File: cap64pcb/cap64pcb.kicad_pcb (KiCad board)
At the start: 2 copper layers, 91.6 x 12 mm, 31 parts, among them J1 SM04B_SURS_TF, Q1 BSS138, Q2 BSS138, U1 MPR121QR2, U2 SPX3819-3.3

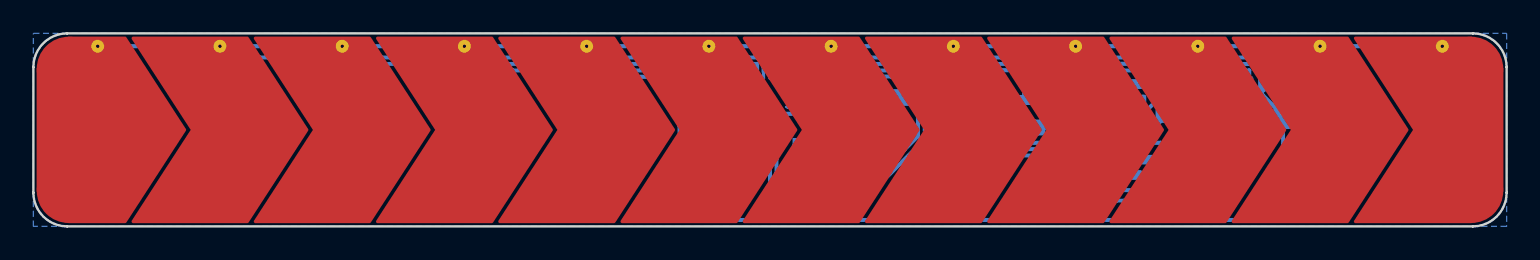
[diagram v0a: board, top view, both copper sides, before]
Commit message: half filleted
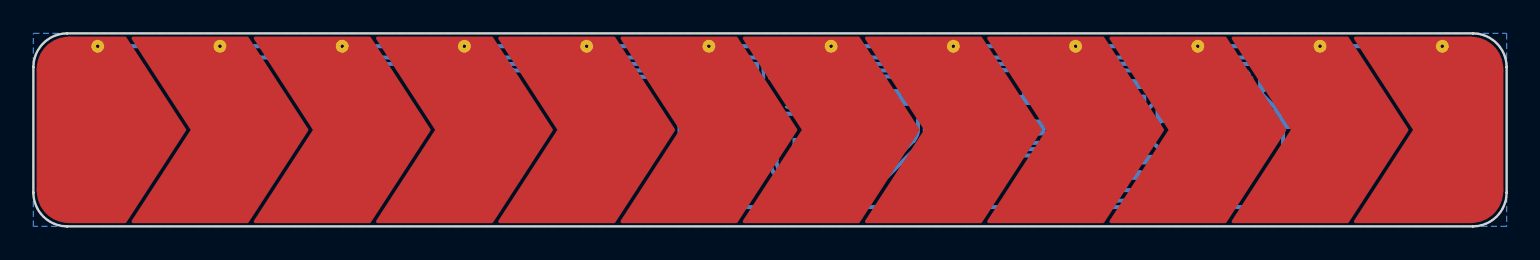
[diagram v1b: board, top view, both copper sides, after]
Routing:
- net GND: track 86.7 -> 82.9 mm
- net Net-(J1-Pad3): track 20.8 -> 19.0 mm
- net Net-(J1-Pad4): track 8.71 -> 7.77 mm
- net SDA: track 28.1 -> 27.5 mm
- net SCL: track 31.5 -> 31.0 mm

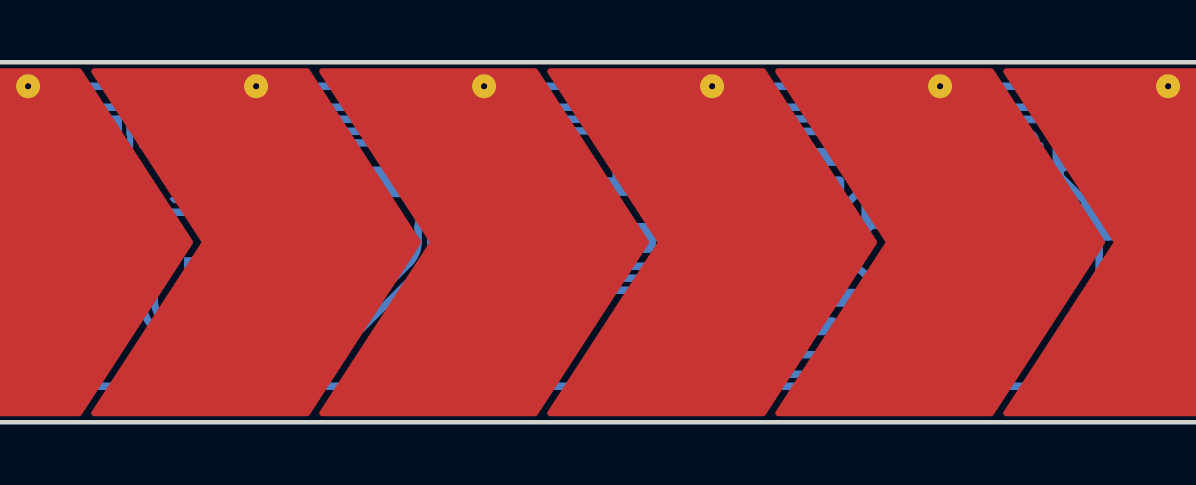
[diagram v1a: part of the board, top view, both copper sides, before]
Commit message: shifted caps/resistors up a smidge
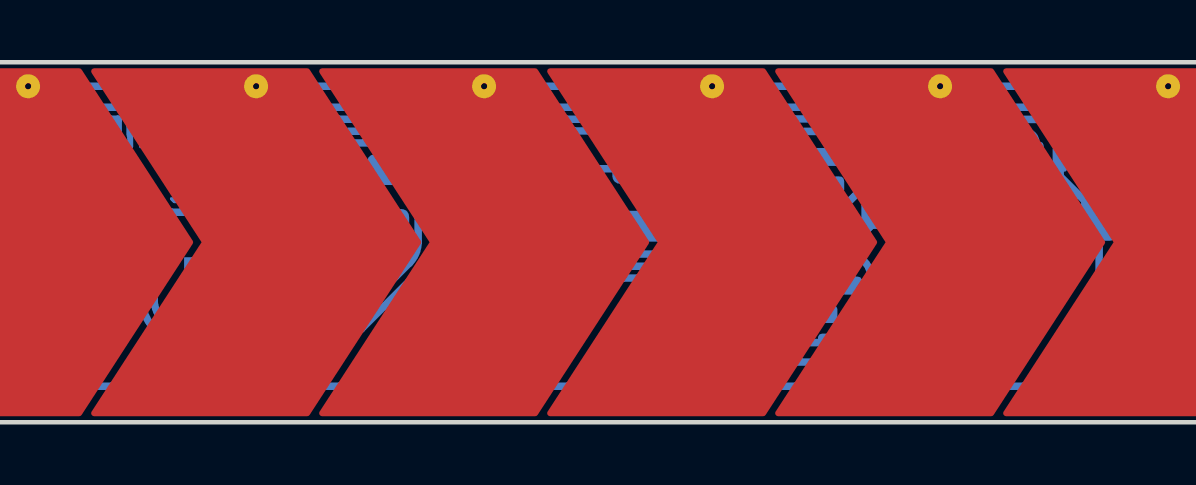
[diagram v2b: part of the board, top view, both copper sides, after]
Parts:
- moved C2 0.41 mm to (98.5, 43.5)
- moved C3 0.41 mm to (96.4, 43.5)
- moved C4 0.41 mm to (94.3, 43.5)
- moved D1 0.41 mm to (85.4, 43.6)
- moved R2 0.41 mm to (92.2, 43.5)
- moved R3 0.41 mm to (90.2, 43.5)
- moved R4 0.41 mm to (88.2, 43.5)
- moved Q1 0.41 mm to (101.5, 47.4)
- moved Q2 0.41 mm to (104.2, 47.4)
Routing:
- net Net-(J1-Pad3): track 19.0 -> 19.9 mm
- net +3V3: track 42.4 -> 43.2 mm
- net Net-(J1-Pad4): track 7.77 -> 8.31 mm

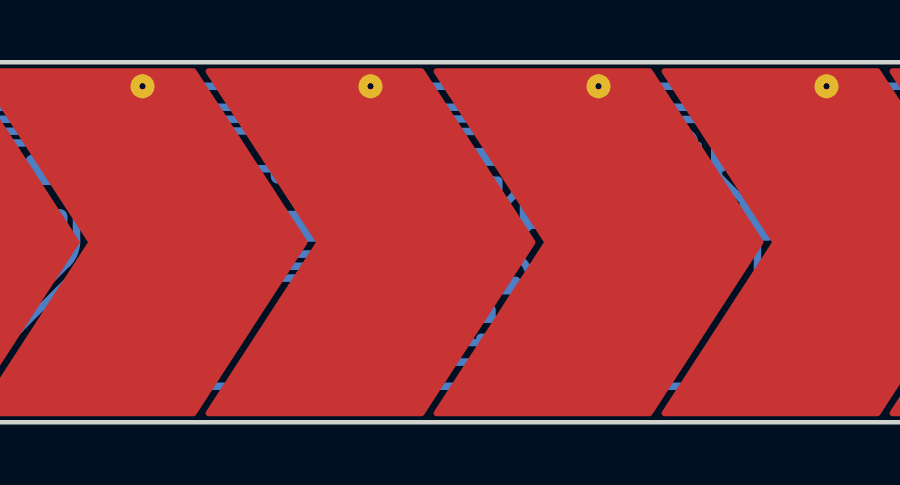
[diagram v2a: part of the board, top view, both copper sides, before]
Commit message: reconnect cap gnd pins
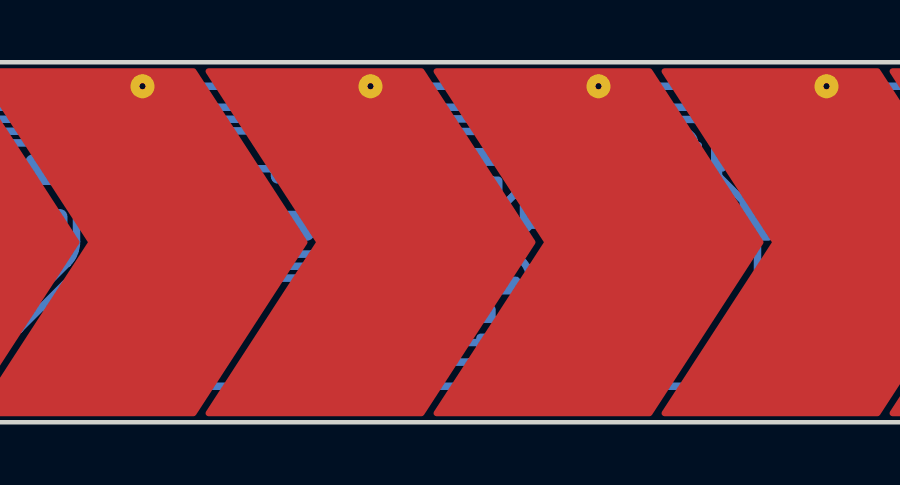
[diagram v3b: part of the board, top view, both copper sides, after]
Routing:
- net Net-(J1-Pad3): track 19.9 -> 18.6 mm
- net Net-(J1-Pad4): track 8.31 -> 7.37 mm
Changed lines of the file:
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@@
   (segment (start 104.7 44.055723) (end 104.05 44.705723) (width 0.25) (layer "B.Cu") (net 2))
   (segment (start 74.45 47.4) (end 75.4 47.4) (width 0.25) (layer "B.Cu") (net 2))
+  (segment (start 101.6 44.705723) (end 98.755723 44.705723) (width 0.25) (layer "B.Cu") (net 2))
   (segment (start 74.45 45.4) (end 74.75 45.1) (width 0.25) (layer "B.Cu") (net 2))
-  (segment (start 101.6 44.705723) (end 101.45 44.855723) (width 0.25) (layer "B.Cu") (net 2))
+  (segment (start 98.5 44.45) (end 96.4 44.45) (width 0.25) (layer "B.Cu") (net 2))
   (segment (start 75.6875 44.1) (end 74.7875 43.2) (width 0.25) (layer "B.Cu") (net 2))
   (segment (start 104.744277 44.1) (end 104.7 44.055723) (width 0.25) (layer "B.Cu") (net 2))
   (segment (start 107.294277 41.305723) (end 101.6 41.305723) (width 0.25) (layer "B.Cu") (net 2))
+  (segment (start 98.755723 44.705723) (end 98.5 44.45) (width 0.25) (layer "B.Cu") (net 2))
   (segment (start 78.1125 44.1) (end 75.6875 44.1) (width 0.25) (layer "B.Cu") (net 2))
   (segment (start 104.05 44.705723) (end 101.6 44.705723) (width 0.25) (layer "B.Cu") (net 2))
+  (segment (start 96.4 44.45) (end 94.3 44.45) (width 0.25) (layer "B.Cu") (net 2))
   (segment (start 110.6 42.15) (end 110.6 42.8) (width 0.25) (layer "B.Cu") (net 2))
   (segment (start 107.694277 40.905723) (end 107.294277 41.305723) (width 0.25) (layer "B.Cu") (net 2))
   (segment (start 74.45 47.4) (end 74.45 45.4) (width 0.25) (layer "B.Cu") (net 2))
   (segment (start 102.7375 43.105723) (end 101.6 43.105723) (width 0.25) (layer "B.Cu") (net 2))
-  (segment (start 96.4 44.855723) (end 94.3 44.855723) (width 0.25) (layer "B.Cu") (net 2))
   (segment (start 74.75 45.0375) (end 75.6875 44.1) (width 0.25) (layer "B.Cu") (net 2))
-  (segment (start 101.45 44.855723) (end 98.5 44.855723) (width 0.25) (layer "B.Cu") (net 2))
   (segment (start 110.6 42.8) (end 111.9 44.1) (width 0.25) (layer "B.Cu") (net 2))
-  (segment (start 98.5 44.855723) (end 96.4 44.855723) (width 0.25) (layer "B.Cu") (net 2))
   (segment (start 111.9 44.1) (end 111.9 47.8) (width 0.25) (layer "B.Cu") (net 2))
   (segment (start 106.9 44.1) (end 104.744277 44.1) (width 0.25) (layer "B.Cu") (net 2))
@@
   (segment (start 103.892893 48.994277) (end 100 48.994277) (width 0.25) (layer "B.Cu") (net 6))
   (segment (start 99.5 48.494277) (end 99.5 47.894277) (width 0.25) (layer "B.Cu") (net 6))
-  (segment (start 109 42.15) (end 109 48.194277) (width 0.25) (layer "B.Cu") (net 6))
+  (segment (start 109 42.15) (end 109 45.394277) (width 0.25) (layer "B.Cu") (net 6))
   (segment (start 100 47.394277) (end 102.4375 47.394277) (width 0.25) (layer "B.Cu") (net 6))
-  (segment (start 109 48.194277) (end 105.107107 48.194277) (width 0.25) (layer "B.Cu") (net 6))
+  (segment (start 106.2 48.194277) (end 105.107107 48.194277) (width 0.25) (layer "B.Cu") (net 6))
   (arc (start 104.246447 48.84783) (mid 104.084235 48.956217) (end 103.892893 48.994277) (width 0.25) (layer "B.Cu") (net 6))
   (arc (start 100 48.994277) (mid 99.646447 48.84783) (end 99.5 48.494277) (width 0.25) (layer "B.Cu") (net 6))
   (arc (start 99.5 47.894277) (mid 99.646447 47.540724) (end 100 47.394277) (width 0.25) (layer "B.Cu") (net 6))
+  (arc (start 109 45.394277) (mid 108.179899 47.374176) (end 106.2 48.194277) (width 0.25) (layer "B.Cu") (net 6))
   (arc (start 105.107107 48.194277) (mid 104.915766 48.232337) (end 104.753554 48.340723) (width 0.25) (layer "B.Cu") (net 6))
   (segment (start 79 47.4) (end 79.5 46.9) (width 0.25) (layer "B.Cu") (net 7))
@@
   (segment (start 86.3375 43.594277) (end 86.973286 43.594277) (width 0.25) (layer "B.Cu") (net 23))
   (arc (start 87.680393 43.88717) (mid 87.35597 43.670397) (end 86.973286 43.594277) (width 0.25) (layer "B.Cu") (net 23))
-  (segment (start 108.2 42.15) (end 108.2 47.394277) (width 0.25) (layer "B.Cu") (net 24))
-  (segment (start 108.2 47.394277) (end 105.137501 47.394277) (width 0.25) (layer "B.Cu") (net 24))
+  (segment (start 108.2 42.15) (end 108.2 45.394277) (width 0.25) (layer "B.Cu") (net 24))
+  (segment (start 106.2 47.394277) (end 105.137501 47.394277) (width 0.25) (layer "B.Cu") (net 24))
+  (arc (start 108.2 45.394277) (mid 107.614214 46.808491) (end 106.2 47.394277) (width 0.25) (layer "B.Cu") (net 24))
   (segment (start 79.6 44.1875) (end 79.6 45) (width 0.25) (layer "B.Cu") (net 25))
   (segment (start 79.6 45) (end 77.2 47.4) (width 0.25) (layer "B.Cu") (net 25))

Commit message: mpr121 3d model
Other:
- board text added: "SM04B- SURS-TF"
- board text added: "["
- board text added: "]"
- board text added: "abcd"
- board text removed: "[abcd]"
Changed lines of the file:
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@@
           ) (width 0.08) (fill yes))
       ))
-    (model "${KICAD6_3DMODEL_DIR}/Package_DFN_QFN.3dshapes/UQFN-20_3x3mm_P0.4mm.wrl"
+    (model "${KICAD6_3DMODEL_DIR}/Package_DFN_QFN.3dshapes/UQFN-20-1EP_3x3mm_P0.4mm_EP1.85x1.85mm.step"
       (offset (xyz 0 0 0))
       (scale (xyz 1 1 1))
@@
       (effects (font (size 1 1) (thickness 0.15)) (justify mirror))
     )
-    (fp_text user "c" (at 1.8 1.8 180) (layer "B.SilkS")
+    (fp_text user "c" (at 1.7 1.8 180) (layer "B.SilkS")
       (effects (font (size 1.2 1.2) (thickness 0.3)) (justify mirror))
     )
@@
       (effects (font (size 1 1) (thickness 0.15)) (justify mirror))
     )
-    (fp_text value "BSS138" (at 5.199999 1.8) (layer "B.SilkS")
+    (fp_text value "BSS138" (at -1.650001 2.605723) (layer "B.SilkS")
       (effects (font (size 1.2 1.2) (thickness 0.3)) (justify mirror))
     )
@@
       (effects (font (size 1.2 1.2) (thickness 0.3)) (justify mirror))
     )
-    (fp_text value "SM04B_SURS_TF" (at -8.9 1.2) (layer "B.SilkS")
+    (fp_text value "SM04B_SURS_TF" (at -8.4 3.3) (layer "B.Fab")
       (effects (font (size 1.2 1.2) (thickness 0.3)) (justify mirror))
     )
@@
     (pad "MP" smd roundrect (at -2.5 -0.8 180) (size 1.2 1.7) (layers "B.Cu" "B.Paste" "B.Mask") (roundrect_rratio 0.208333)
       (net 2 "GND") (pinfunction "MP") (pintype "power_in"))
-    (model "${KICAD6_3DMODEL_DIR}/Connector_JST.3dshapes/JST_SUR_SM04B-SURS-TF_1x04-1MP_P0.80mm_Horizontal.wrl"
-      (offset (xyz 0 0 0))
-      (scale (xyz 1 1 1))
-      (rotate (xyz 0 0 0))
-    )
   )
   (gr_arc (start 101.1 39.9) (mid 101.524264 40.075736) (end 101.7 40.5) (layer "B.SilkS") (width 0.2))
@@
     (effects (font (size 1 1) (thickness 0.2)) (justify mirror))
   )
+  (gr_text "0x5" (at 72.9 47.4) (layer "B.SilkS")
+    (effects (font (size 1.2 1.2) (thickness 0.3)) (justify mirror))
+  )
   (gr_text "sda" (at 108.6 46.8 90) (layer "B.SilkS")
     (effects (font (size 1 1) (thickness 0.2)) (justify mirror))
   )
-  (gr_text "biddle" (at 54.4 46) (layer "B.SilkS")
+  (gr_text "biddle" (at 52.6 46) (layer "B.SilkS")
     (effects (font (size 1.5 1.5) (thickness 0.3)) (justify mirror))
   )
@@
     (effects (font (size 1 1) (thickness 0.2)) (justify mirror))
   )
-  (gr_text "64" (at 56.4 43.7) (layer "B.SilkS")
+  (gr_text "SM04B-\nSURS-TF" (at 121.6 43.4) (layer "B.SilkS")
+    (effects (font (size 1.2 1.2) (thickness 0.3)) (justify left mirror))
+  )
+  (gr_text "64" (at 54.6 43.7) (layer "B.SilkS")
     (effects (font (size 1.5 1.5) (thickness 0.3)) (justify mirror))
   )
-  (gr_text "[abcd]" (at 117.5 44.8) (layer "B.SilkS")
+  (gr_text "abcd" (at 68.4 47.4) (layer "B.SilkS")
     (effects (font (size 1.2 1.2) (thickness 0.3)) (justify mirror))
   )
-  (gr_text "cap" (at 59.9 43.7) (layer "B.Mask")
+  (gr_text "cap" (at 58.1 43.7) (layer "B.Mask")
     (effects (font (size 1.5 1.5) (thickness 0.3)) (justify mirror))
   )
-  (gr_text "0x5" (at 122 44.8) (layer "B.Mask")
+  (gr_text "[" (at 70.9 47.3) (layer "B.Mask")
     (effects (font (size 1.2 1.2) (thickness 0.3)) (justify mirror))
   )
-  (gr_text "beady" (at 61.2 46) (layer "B.Mask")
+  (gr_text "]" (at 65.9 47.3) (layer "B.Mask")
+    (effects (font (size 1.2 1.2) (thickness 0.3)) (justify mirror))
+  )
+  (gr_text "beady" (at 59.4 46) (layer "B.Mask")
     (effects (font (size 1.5 1.5) (thickness 0.3)) (justify mirror))
   )
@@
     )
   )
+  (group "" (id 276355c2-5f92-4a10-aa56-8aeebc711e2d)
+    (members
+      50d2e643-d251-40d5-a3e9-7b446448ecba
+      9e506fbd-ce5d-47f1-a521-e7d9db5ecfb6
+      a8b0c6ad-c126-4ac4-bb8f-96b00030c899
+      f4c857c9-4d89-447a-8a69-cf9da90c7188
+    )
+  )
+  (group "" (id 479919e5-5469-4d3f-aad5-0b54dff5bcad)
+    (members
+      57031c67-5381-436f-87fb-abcea6a67a15
+      ea0010ea-9bdc-4bdb-b60d-e35099ae79fc
+    )
+  )
+  (group "" (id 78375fc6-14c5-4e2f-be5c-8daab93573cc)
+    (members
+      6f42b7e3-3a3c-4bc0-901a-9101873762cd
+      cb072ea9-fafb-47b8-8232-8a2061a729f2
+    )
+  )
